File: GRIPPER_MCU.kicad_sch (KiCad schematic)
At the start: 2 parts, among them IC16 STM32G030K8T6

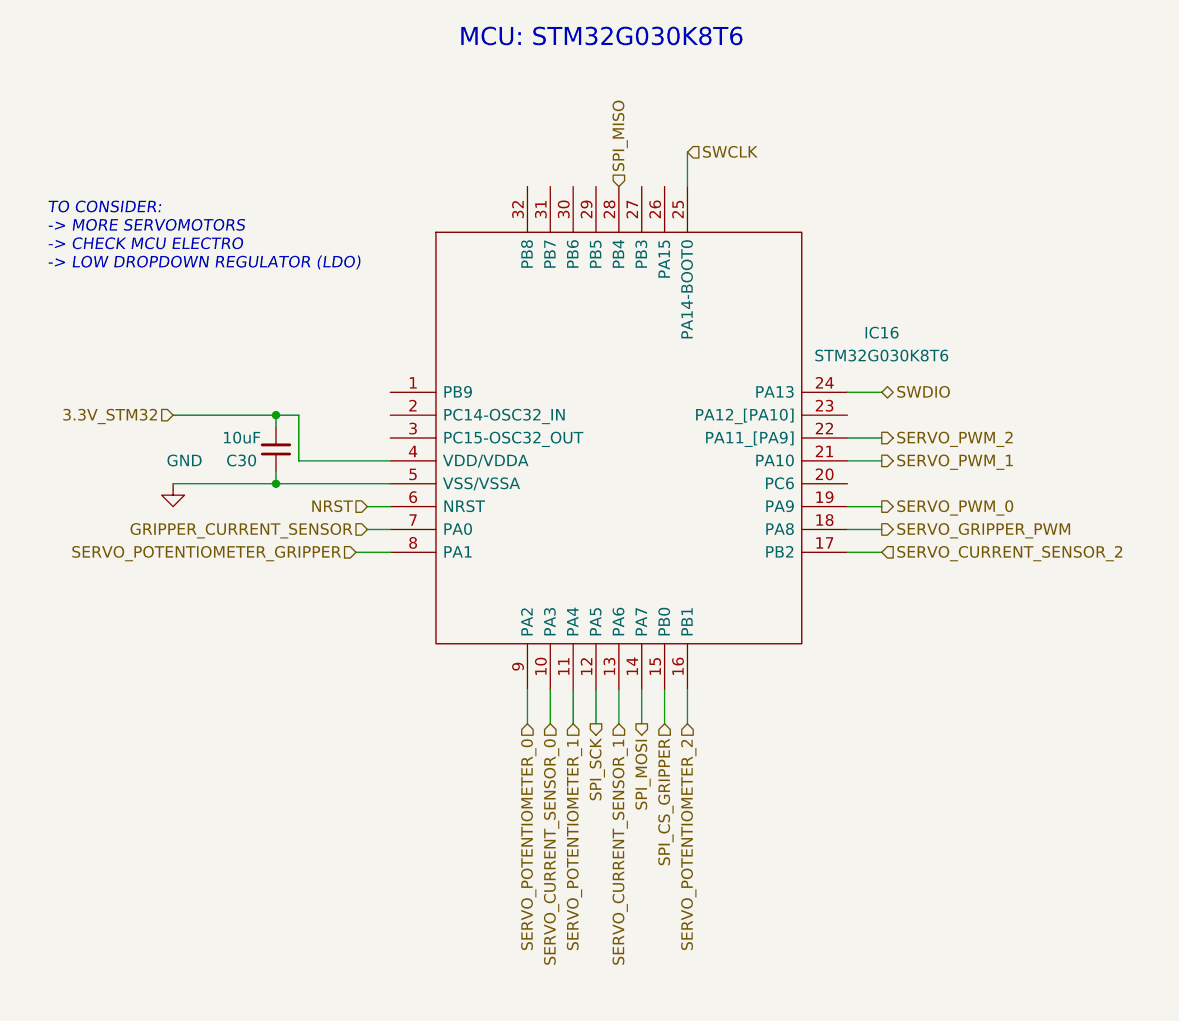
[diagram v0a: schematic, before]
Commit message: Bord v1.2, added flash memory, changed pinout od servomotor connectors and removed potentiometer signal from servomotors plus one ADC
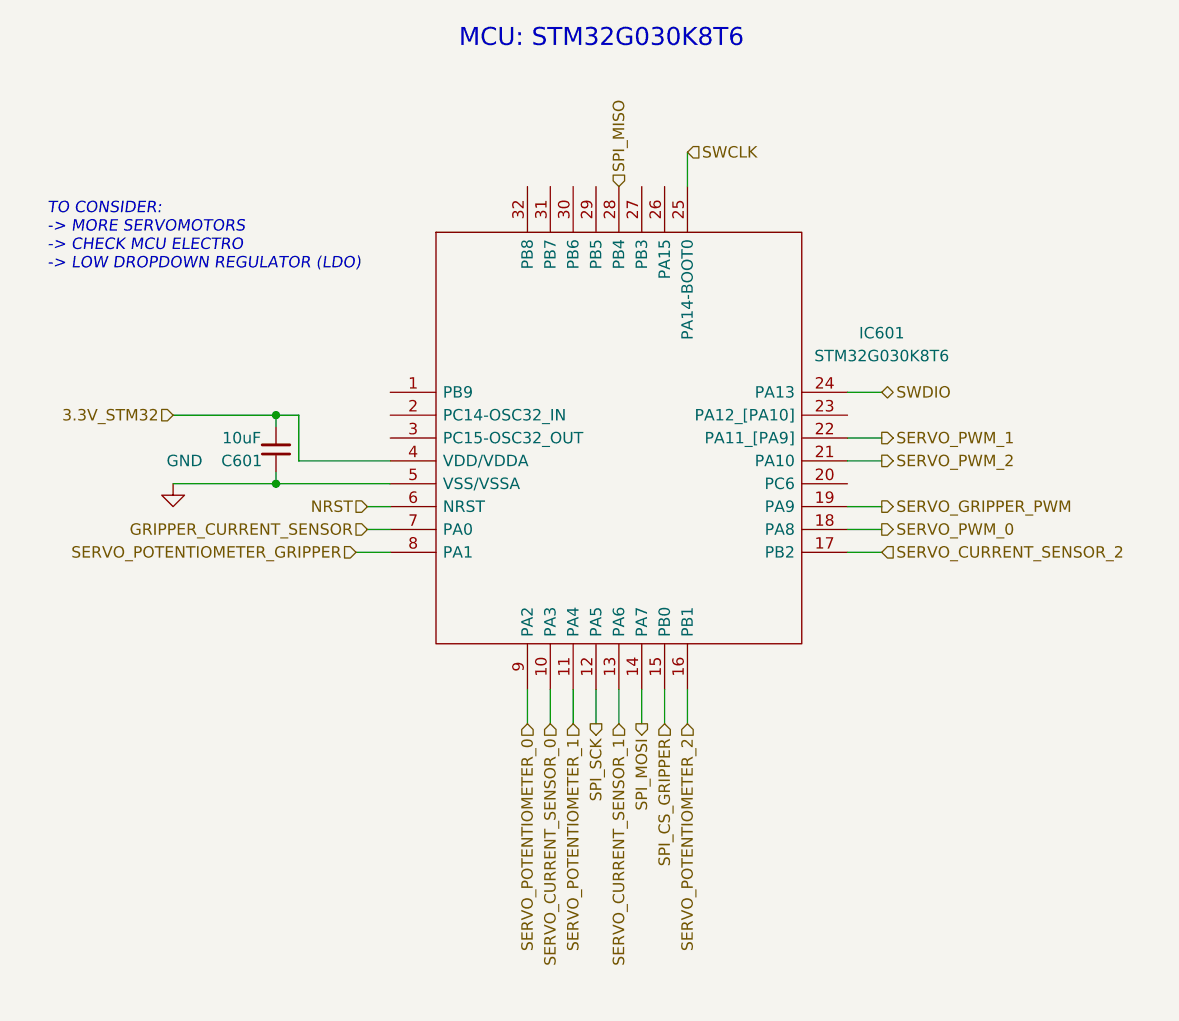
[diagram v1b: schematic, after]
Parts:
- renumbered C30 to C601, IC16 to IC601
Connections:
- net SERVO_GRIPPER_PWM: now also IC601.19 (PA9); no longer IC601.18 (PA8)
- net SERVO_PWM_0: now also IC601.18 (PA8); no longer IC601.19 (PA9)
- net SERVO_PWM_1: now also IC601.22 (PA11_[PA9]); no longer IC601.21 (PA10)
- net SERVO_PWM_2: now also IC601.21 (PA10); no longer IC601.22 (PA11_[PA9])
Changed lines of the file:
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@@
     )
+  )
+  (hierarchical_label "SERVO_PWM_1" (shape output) (at 170.18 95.25 0) (fields_autoplaced)
+    (effects (font (size 1.27 1.27)) (justify left))
   )
   (hierarchical_label "SPI_MISO" (shape input) (at 140.97 67.31 90) (fields_autoplaced)
@@
     )
   )
-  (hierarchical_label "SERVO_PWM_2" (shape output) (at 170.18 95.25 0) (fields_autoplaced)
+  (hierarchical_label "SERVO_PWM_0" (shape output) (at 170.18 105.41 0) (fields_autoplaced)
     (effects (font (size 1.27 1.27)) (justify left))
   )
@@
     (effects (font (size 1.27 1.27)) (justify right))
   )
+  (hierarchical_label "SERVO_GRIPPER_PWM" (shape output) (at 170.18 102.87 0) (fields_autoplaced)
+    (effects (font (size 1.27 1.27)) (justify left))
+    (property "Intersheetrefs" "${INTERSHEET_REFS}" (at 192.5827 102.87 0)
+      (effects (font (size 1.27 1.27)) (justify left) hide)
+    )
+  )
   (hierarchical_label "SWCLK" (shape input) (at 148.59 63.5 0) (fields_autoplaced)
     (effects (font (size 1.27 1.27)) (justify left))
@@
     (effects (font (size 1.27 1.27)) (justify right))
   )
-  (hierarchical_label "SERVO_GRIPPER_PWM" (shape output) (at 170.18 105.41 0) (fields_autoplaced)
-    (effects (font (size 1.27 1.27)) (justify left))
-    (property "Intersheetrefs" "${INTERSHEET_REFS}" (at 192.5827 105.41 0)
-      (effects (font (size 1.27 1.27)) (justify left) hide)
-    )
-  )
-  (hierarchical_label "SERVO_PWM_0" (shape output) (at 170.18 102.87 0) (fields_autoplaced)
-    (effects (font (size 1.27 1.27)) (justify left))
-  )
   (hierarchical_label "SERVO_CURRENT_SENSOR_1" (shape input) (at 140.97 127 270) (fields_autoplaced)
     (effects (font (size 1.27 1.27)) (justify right))
@@
     (effects (font (size 1.27 1.27)) (justify right))
   )
+  (hierarchical_label "SERVO_PWM_2" (shape output) (at 170.18 97.79 0) (fields_autoplaced)
+    (effects (font (size 1.27 1.27)) (justify left))
+  )
   (hierarchical_label "SPI_CS_GRIPPER" (shape input) (at 146.05 127 270) (fields_autoplaced)
     (effects (font (size 1.27 1.27)) (justify right))
@@
       (effects (font (size 1.27 1.27)) (justify right) hide)
     )
-  )
-  (hierarchical_label "SERVO_PWM_1" (shape output) (at 170.18 97.79 0) (fields_autoplaced)
-    (effects (font (size 1.27 1.27)) (justify left))
   )
   (hierarchical_label "SERVO_POTENTIOMETER_2" (shape input) (at 148.59 127 270) (fields_autoplaced)
@@
   (symbol (lib_id "Device:C_Small") (at 102.87 96.52 180) (unit 1)
     (in_bom yes) (on_board yes) (dnp no)
-    (property "Reference" "C30" (at 99.06 97.79 0)
+    (property "Reference" "C601" (at 99.06 97.79 0)
       (effects (font (size 1.27 1.27)))
     )
@@
     (instances
       (project "Hexapod_Hardware"
-        (path "/04005f68-61ba-4735-aba3-9cac296c0cce/131ce24a-6b68-4bf4-9124-91468713a7c9"
-          (reference "C30") (unit 1)
-        )
-        (path "/04005f68-61ba-4735-aba3-9cac296c0cce/131ce24a-6b68-4bf4-9124-91468713a7c9/2866b240-bcad-4f09-afcc-1811f3d507a8"
-          (reference "C8") (unit 1)
+        (path "/04005f68-61ba-4735-aba3-9cac296c0cce/2cd4ba25-52d1-4db4-b74d-e04810e070ce/59004b94-8694-4dc2-864b-96bb314c80e0/2866b240-bcad-4f09-afcc-1811f3d507a8"
+          (reference "C601") (unit 1)
         )
       )
@@
   (symbol (lib_id "STM32G030K8T6:STM32G030K8T6") (at 115.57 90.17 0) (unit 1)
     (in_bom yes) (on_board yes) (dnp no) (fields_autoplaced)
-    (property "Reference" "IC16" (at 170.18 83.5912 0)
+    (property "Reference" "IC601" (at 170.18 83.5912 0)
       (effects (font (size 1.27 1.27)))
     )
@@
     (instances
       (project "Hexapod_Hardware"
-        (path "/04005f68-61ba-4735-aba3-9cac296c0cce/131ce24a-6b68-4bf4-9124-91468713a7c9"
-          (reference "IC16") (unit 1)
-        )
-        (path "/04005f68-61ba-4735-aba3-9cac296c0cce/131ce24a-6b68-4bf4-9124-91468713a7c9/2866b240-bcad-4f09-afcc-1811f3d507a8"
-          (reference "IC4") (unit 1)
+        (path "/04005f68-61ba-4735-aba3-9cac296c0cce/2cd4ba25-52d1-4db4-b74d-e04810e070ce/59004b94-8694-4dc2-864b-96bb314c80e0/2866b240-bcad-4f09-afcc-1811f3d507a8"
+          (reference "IC601") (unit 1)
         )
       )
@@
   (symbol (lib_id "power:GND") (at 91.44 100.33 0) (unit 1)
     (in_bom yes) (on_board yes) (dnp no)
-    (property "Reference" "#PWR0131" (at 91.44 106.68 0)
+    (property "Reference" "#PWR0601" (at 91.44 106.68 0)
       (effects (font (size 1.27 1.27)) hide)
     )
@@
     (instances
       (project "Hexapod_Hardware"
-        (path "/04005f68-61ba-4735-aba3-9cac296c0cce/131ce24a-6b68-4bf4-9124-91468713a7c9"
-          (reference "#PWR0131") (unit 1)
-        )
-        (path "/04005f68-61ba-4735-aba3-9cac296c0cce/131ce24a-6b68-4bf4-9124-91468713a7c9/2866b240-bcad-4f09-afcc-1811f3d507a8"
-          (reference "#PWR083") (unit 1)
-        )
-      )
+        (path "/04005f68-61ba-4735-aba3-9cac296c0cce/2cd4ba25-52d1-4db4-b74d-e04810e070ce/59004b94-8694-4dc2-864b-96bb314c80e0/2866b240-bcad-4f09-afcc-1811f3d507a8"
+          (reference "#PWR0601") (unit 1)
+        )
+      )
